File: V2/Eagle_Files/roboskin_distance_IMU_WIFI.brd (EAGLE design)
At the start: 43.2 x 33 mm, 41 parts, among them IC1 CP2104, Q1 mmbt2222, Q2 mmbt2222, SW2 KMR2, U2 AP2112-3.3, U3 MCP73831T-2ACI/OT, U4 LSM6DS3DOT_INDICATION, U5 VL53L1XSMD, X1 JSTPH, X2 ESP-12, X4 20329

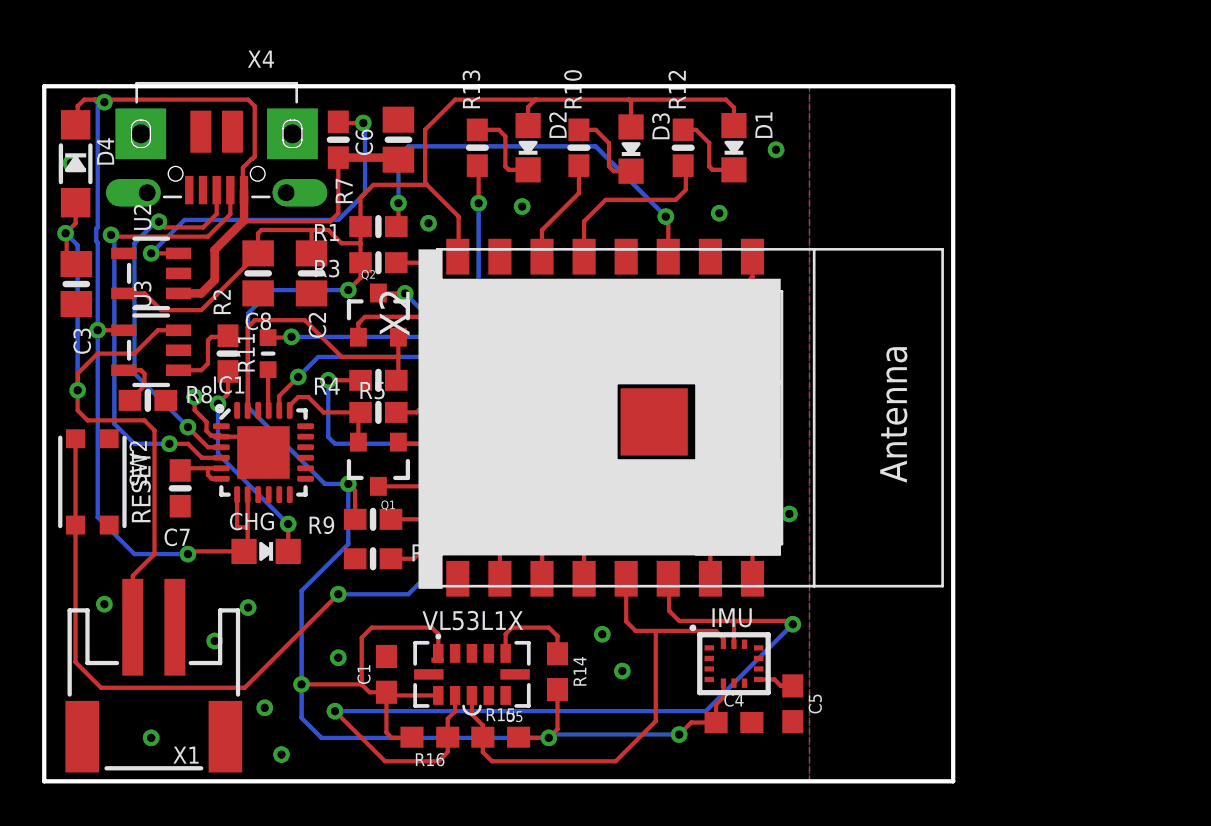
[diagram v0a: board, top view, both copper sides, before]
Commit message: updating v2 with new accelerometer and adding a power switch
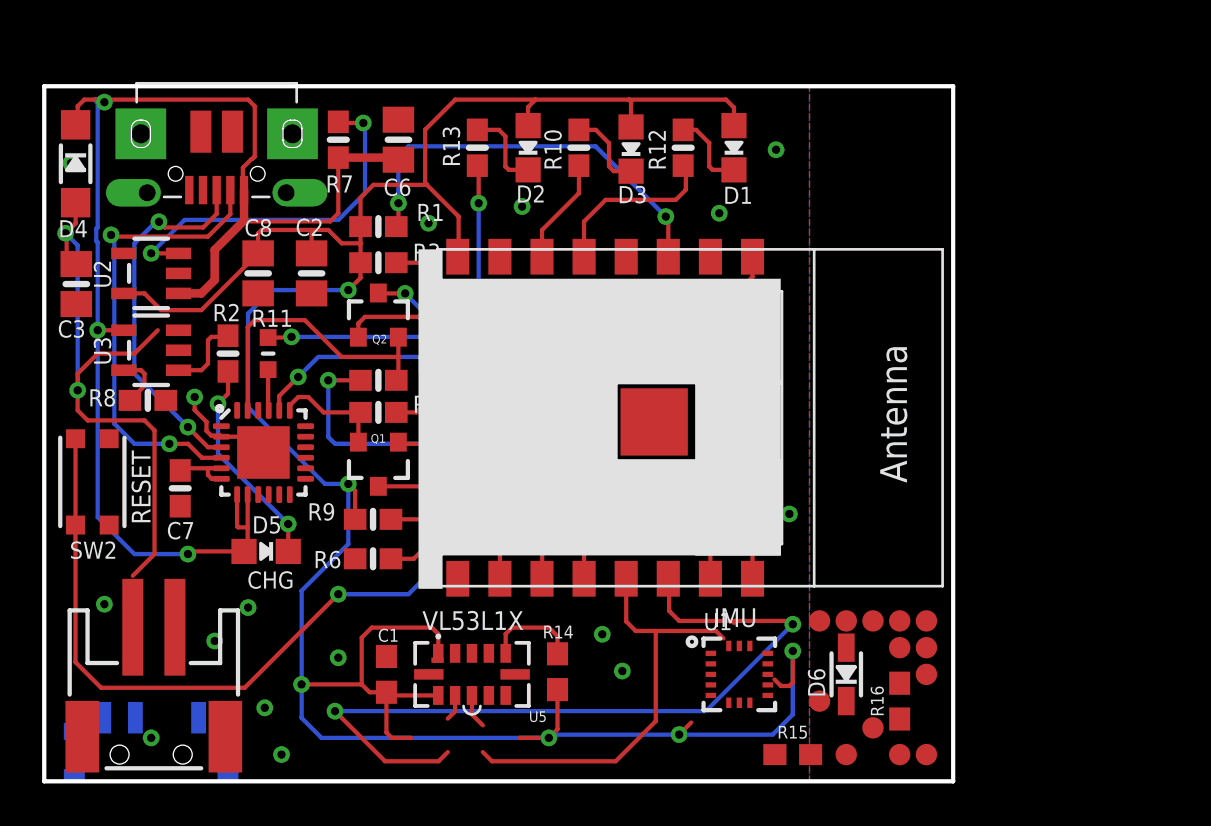
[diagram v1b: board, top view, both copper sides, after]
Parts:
- removed C4, C5: 0.1uF, SparkFun-Capacitors:0603
- removed U4: LSM6DS3DOT_INDICATION, LSM6DS3:LGA14L_DOT_INDICATOR
- added D6: 1N4148, microbuilder:SOD-323
- added S1: (no value), SparkFun-Switches:SWITCH_SPST_SMD_A
- added TP1, TP10, TP11, TP12, TP13, TP2, TP3, TP4, TP5, TP6, TP7, TP8, TP9: TEST-POINT3X4, SparkFun-Connectors:PAD.03X.04
- added U1: LIS3DHTR, microbuilder:LGA16_3X3MM
- D5: value ORANGE -> CHG
- R15, R16: value 4.7k -> 10k
- U3: value MCP73831T-2ACI/OT -> MCP
- moved R16 22.4 mm to (40.6, 3.81), turned to 90 degrees
- moved R15 13.9 mm to (35.6, 1.27)
- renumbered CHG to D5
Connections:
- removed net N$14: C5.1, U4.8
- new net CS: D6.C
- new net N$7: D6.A, R15.2, U1.8
- new net SDO: R16.2, U1.7
- new net V_CHARGE: C3.1, S1.3, U3.3, X1.2
- net 3.3V: now also R15.1, U1.1, U1.14, U1.15; no longer C4.1, R15.2, R16.2, U4.5
- net GND: now also R16.1, U1.10, U1.12, U1.13, U1.16, U1.5; no longer C4.2, C5.2, U4.1, U4.2, U4.3, U4.6, U4.7
- net SCL: now also U1.4; no longer R16.1, U4.13
- net SDA: now also U1.6; no longer R15.1, U4.14
- net VBAT: now also S1.2; no longer C3.1, U3.3, X1.2
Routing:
- net 3.3V: track 122.0 -> 130.0 mm, vias 5 -> 6
- net VBAT: track 32.3 -> 28.2 mm
- net SCL: track 41.6 -> 39.0 mm
- net N$14: track 1.75 -> 0.00 mm
- net SDA: track 23.6 -> 22.1 mm

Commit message: All versions of hardware
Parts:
- removed D5: CHG, microbuilder:CHIPLED_0805_NOOUTLINE
- removed S1: (no value), SparkFun-Switches:SWITCH_SPST_SMD_A
- removed TP1, TP10, TP11, TP12, TP13, TP2, TP3, TP4, TP5, TP6, TP7, TP8, TP9: TEST-POINT3X4, SparkFun-Connectors:PAD.03X.04
- removed X1: JSTPH, microbuilder:JSTPH2
- added C4, C5: 0.1uF, SparkFun-Capacitors:0603
- added J1, J10, J2, J3, J4, J6, J7, J8, J9: (no value), SparkFun-Connectors:1X01
- added J5: (no value), SparkFun-Connectors:JST-2-SMD
- added Q3: ZXMP6A13FTA, SparkFun-DiscreteSemi:SOT23-3
- added R17: 100k, SparkFun-Resistors:0603-RES
- added S2: POWER, SparkFun-Electromechanical:SWITCH-SPST-SMD-A
- C2: device microbuilder:0805-NO -> SparkFun-Capacitors:0805
- C3, C6, C8: value 10µF -> 10uF; device microbuilder:0805-NO -> SparkFun-Capacitors:0805
- C7: value 1uF -> 1.0uF; device microbuilder:0603-NO -> SparkFun-Capacitors:0603
- D1, D2, D3: value RED -> WHITE; device microbuilder:CHIPLED_0805_NOOUTLINE -> SparkFun-LED:LED-1206
- D4: value MBR120 -> WHITE; device microbuilder:SOD-123 -> SparkFun-LED:LED-1206
- D6: value 1N4148 -> BAT20J; device microbuilder:SOD-323 -> SparkFun-DiscreteSemi:SOD-323
- R1, R3, R4, R5, R7, R9: value 10K -> 10k; device microbuilder:0603-NO -> SparkFun-Resistors:0603
- R10, R12, R13, R2, R8: value 1K -> 1k; device microbuilder:0603-NO -> SparkFun-Resistors:0603
- R11: value 1K -> 1k; device microbuilder:_0603MP -> SparkFun-Resistors:0603
- R15, R16: value 10k -> 4.7k
- R6: value 4.7K -> 4.7k; device microbuilder:0603-NO -> SparkFun-Resistors:0603
- U1: value LIS3DHTR -> ISM330DLCTR; device microbuilder:LGA16_3X3MM -> ISM330:LGA-14L_2P5X3X0P83_STM
- moved D6 36.9 mm to (10.8, 29.8), turned to 180 degrees
- moved R1 21.8 mm to (37.1, 31.1), turned to 270 degrees
- moved C3 18.1 mm to (14.5, 11.0), turned to 0 degrees
- moved D4 17.5 mm to (14.6, 17.8), turned to 180 degrees
- moved SW2 16.2 mm to (16.3, 5.97)
- moved R3 15.4 mm to (22.5, 10.8), turned to 0 degrees
- moved R8 14.7 mm to (19.4, 15.6)
- moved U2 14.0 mm to (16.8, 31.8)
- moved C7 12.6 mm to (13.0, 24.7), turned to 180 degrees
- moved U3 11.3 mm to (14.6, 14.4), turned to 270 degrees
- moved R9 10.5 mm to (26.0, 10.8)
- moved R6 10.5 mm to (26.0, 9.21)
- moved U$6 10.2 mm to (32.1, 18.4)
- moved Q2 10.2 mm to (26.0, 23.4)
- moved X2 10.2 mm to (38.0, 18.5)
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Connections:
- removed net N$10: D2.C, R13.2
- removed net SDO: R16.2, U1.7
- removed net VBAT: D4.A, S1.2
- removed net V_CHARGE: C3.1, S1.3, U3.3, X1.2
- new net INMOSFET: D6.C, Q3.2, S2.3
- new net INT1: J3.1, U1.4
- new net INT2: J2.1, U1.9
- new net LIPO: C3.1, J5.2, Q3.3, U3.3
- new net SDAO: J1.1, U1.1
- new net VDIO: C5.1, U1.5
- new net VINPUT: C6.1, R7.2, S2.2, U2.1
- net 3.3V: now also C4.1, R15.2, R16.2, U1.8; no longer R15.1, U1.1, U1.14, U1.15
- net ADC: now also J6.1
- net CS: now also J4.1, U1.12; no longer D6.C
- net GND: now also C4.2, C5.2, J5.1, R17.1, U1.2, U1.3, U1.6, U1.7; no longer R16.1, U1.10, U1.12, U1.13, U1.16, U1.5, X1.1
- net GPIO13/MOSI: now also J8.1
- net GPIO14: now also J7.1
- net N$1: now also D4.C; no longer D5.C
- net N$5: now also D1.C, R13.2; no longer D3.C, R10.2
- net N$7: now also D2.C, R10.2; no longer D6.A, R15.2, U1.8
- net N$9: now also D3.C; no longer D1.C
- net SCL: now also J9.1, R16.1, U1.13; no longer U1.4
- net SDA: now also J10.1, R15.1, U1.14; no longer U1.6
- net VBUS: now also D4.A, D6.A, Q3.1, R17.2; no longer C6.1, D4.C, D5.A, R7.2, U2.1
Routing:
- net VINPUT: track 0.00 -> 33.0 mm, vias 0 -> 2
- net INMOSFET: track 0.00 -> 31.6 mm, vias 0 -> 3
- net VBAT: track 28.2 -> 0.00 mm, vias 2 -> 0
- net 3.3V: track 130.0 -> 107.5 mm
- net GPIO14: track 8.33 -> 29.1 mm, vias 0 -> 2
- net GPIO13/MOSI: track 0.00 -> 19.3 mm, vias 0 -> 1
- net RESET: track 65.9 -> 47.4 mm, vias 2 -> 0
- net LIPO: track 0.00 -> 16.6 mm
- net CS: track 0.00 -> 16.2 mm, vias 0 -> 1
- net EN: track 17.2 -> 2.93 mm, vias 2 -> 0
- net GND: track 4.97 -> 17.7 mm, vias 22 -> 18
- net INT2: track 0.00 -> 12.7 mm
- net CH_PD: track 19.6 -> 7.31 mm, vias 2 -> 0
- net VDIO: track 0.00 -> 11.6 mm, vias 0 -> 2
- net N$6: track 22.1 -> 11.1 mm, vias 2 -> 0
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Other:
- board size 43.2 x 33 mm -> 50.8 x 33 mm
